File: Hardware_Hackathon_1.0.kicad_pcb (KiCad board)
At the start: 2 copper layers, 50.8 x 22.9 mm, 15 parts, among them J2 Conn_01x04, Q1 BC547, SW1 SW_Push_SPDT

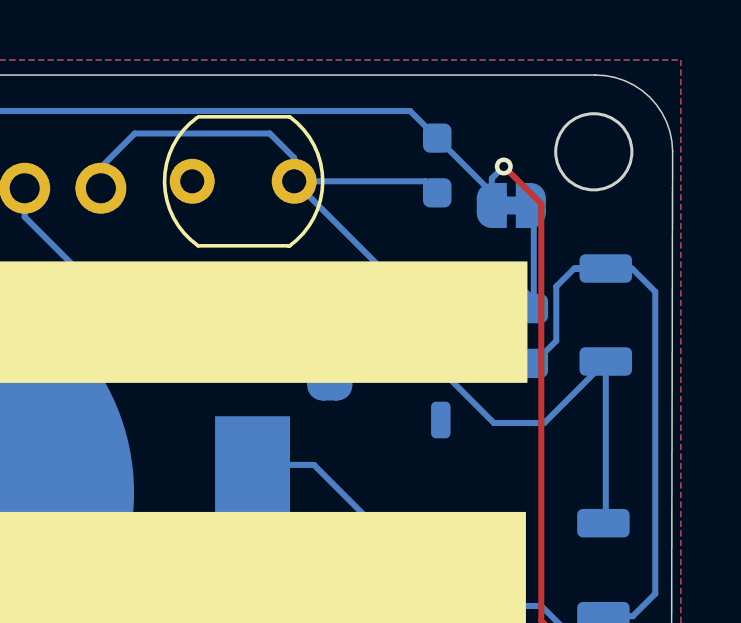
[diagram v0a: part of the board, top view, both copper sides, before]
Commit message: fixed BC817 symbol and footprint pin reversal
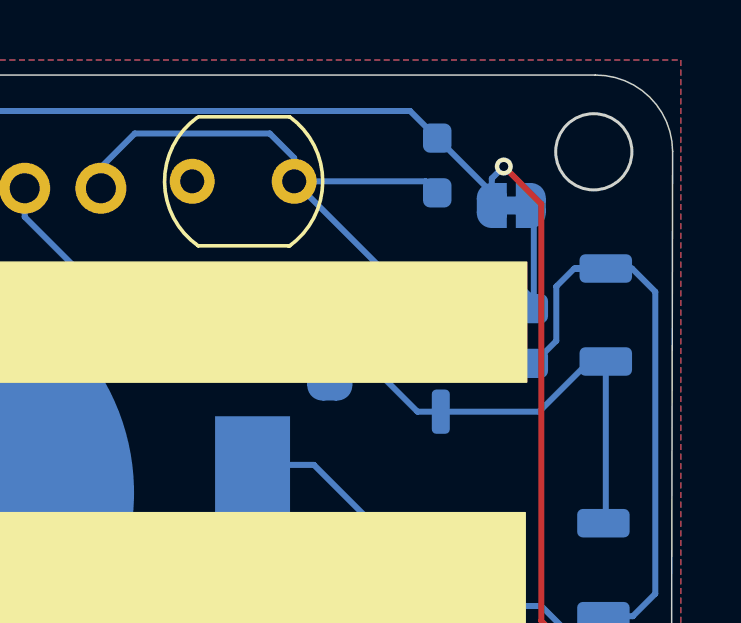
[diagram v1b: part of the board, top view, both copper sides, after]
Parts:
- Q1: value BC547 -> BC817; footprint Package_TO_SOT_SMD:TSOT-23 -> Package_TO_SOT_SMD:SOT-23
- R2: value LDR07 -> 5mm (LDR)
- moved Q1 0.09 mm to (168.0, 105.3)
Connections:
- Q1 pad 1: Net-(D1-K) -> Net-(J2-Pin_4)
- Q1 pad 2: Net-(J2-Pin_4) -> GND
- Q1 pad 3: GND -> Net-(D1-K)
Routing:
- net Net-(J2-Pin_4): track 21.7 -> 21.1 mm
